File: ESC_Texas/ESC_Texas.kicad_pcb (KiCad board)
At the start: 4 copper layers, 118 x 73.2 mm, 165 parts, among them IC1 nRF52840-QFAA-F-R7, IC10 UCC21331CQDRQ1, IC11 LM3480IM3-3.3_NOPB, IC2 UCC21331CQDRQ1, IC3 AD8411AWBRZ, IC4 MC78L05ACHT1G, IC5 AD8411AWBRZ, IC6 MC78L05ACHT1G, IC7 UCC21331CQDRQ1, IC8 AD8411AWBRZ, IC9 MC78L05ACHT1G, J1 Battery-, J10 Conn_01x03_Pin, J11 Conn_01x02_Pin, J12 Conn_01x02, J13 Conn_01x06_Pin, J14 Conn_01x04_Pin, J15 Conn_01x04_Pin, J16 Conn_01x07_Pin, J2 Conn_01x08_Pin, J3 Motor, J4 Battery+, J5 Conn_01x03_Pin, J6 Conn_01x03_Pin, J7 Conn_01x03_Pin, J8 Conn_01x03_Pin, J9 Conn_01x03_Pin, Q1 IPD100N06S4, Q2 IPD100N06S4, Q3 IPD100N06S4, Q4 IPD100N06S4, Q5 IPD100N06S4, Q6 IPD100N06S4, U1 MCP2515-xSO, U2 TJA1051T, X1 C115962, Y1 CM7V-T1A-32.768kHz, Y2 32MHz

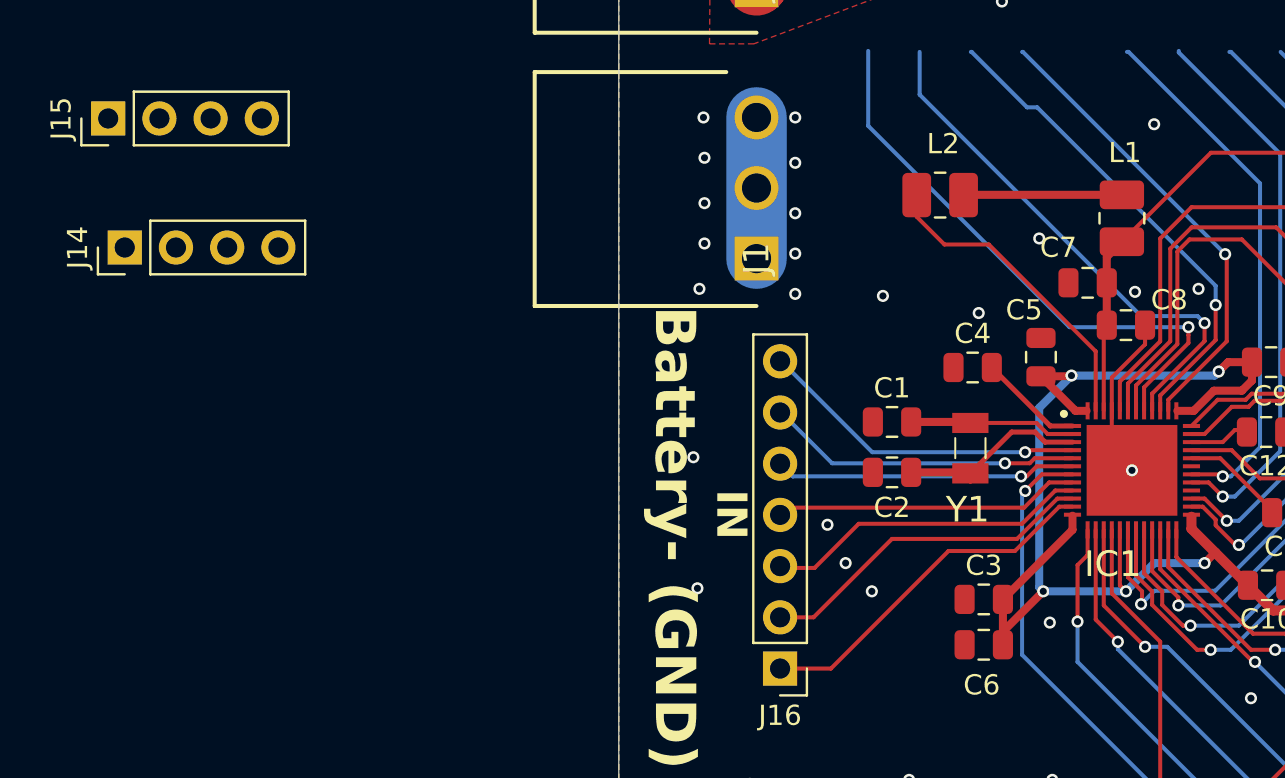
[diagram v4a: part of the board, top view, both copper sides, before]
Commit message: Testpoints instead of hearders
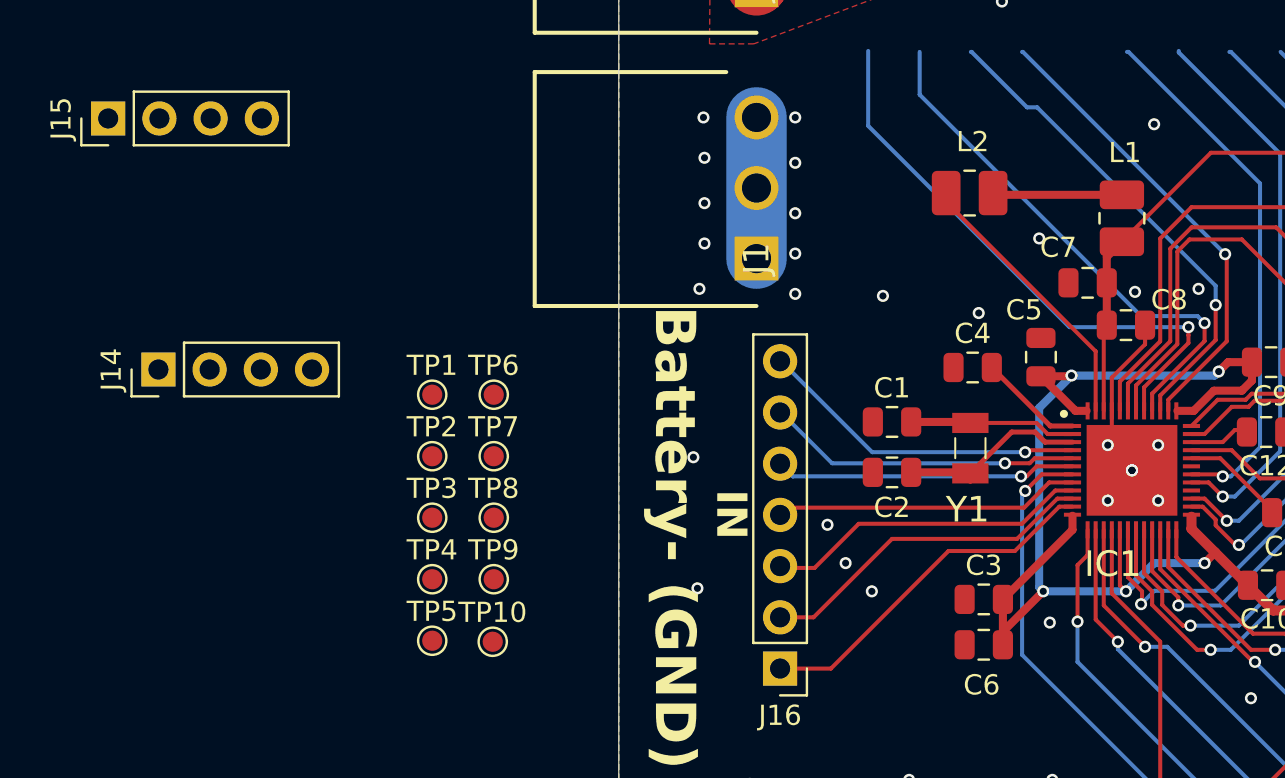
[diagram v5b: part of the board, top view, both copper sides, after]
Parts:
- added TP1: TestPoint, TestPoint:TestPoint_Pad_D1.0mm, F.Cu at (82.8, 111.5)
- added TP10: TestPoint, TestPoint:TestPoint_Pad_D1.0mm, F.Cu at (85.8, 123.8)
- added TP2: TestPoint, TestPoint:TestPoint_Pad_D1.0mm, F.Cu at (82.8, 114.5)
- added TP3: TestPoint, TestPoint:TestPoint_Pad_D1.0mm, F.Cu at (82.8, 117.6)
- added TP4: TestPoint, TestPoint:TestPoint_Pad_D1.0mm, F.Cu at (82.8, 120.7)
- added TP5: TestPoint, TestPoint:TestPoint_Pad_D1.0mm, F.Cu at (82.8, 123.7)
- added TP6: TestPoint, TestPoint:TestPoint_Pad_D1.0mm, F.Cu at (85.8, 111.5)
- added TP7: TestPoint, TestPoint:TestPoint_Pad_D1.0mm, F.Cu at (85.8, 114.5)
- added TP8: TestPoint, TestPoint:TestPoint_Pad_D1.0mm, F.Cu at (85.8, 117.6)
- added TP9: TestPoint, TestPoint:TestPoint_Pad_D1.0mm, F.Cu at (85.8, 120.7)
- moved J14 6.28 mm to (69.2, 110.2)
- moved L2 1.47 mm to (109.4, 101.5)
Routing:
- net Net-(IC1-DCC): track 15.7 -> 13.9 mm
- net Net-(L1-Pad2): track 7.86 -> 6.42 mm
- net GND: vias 202 -> 207

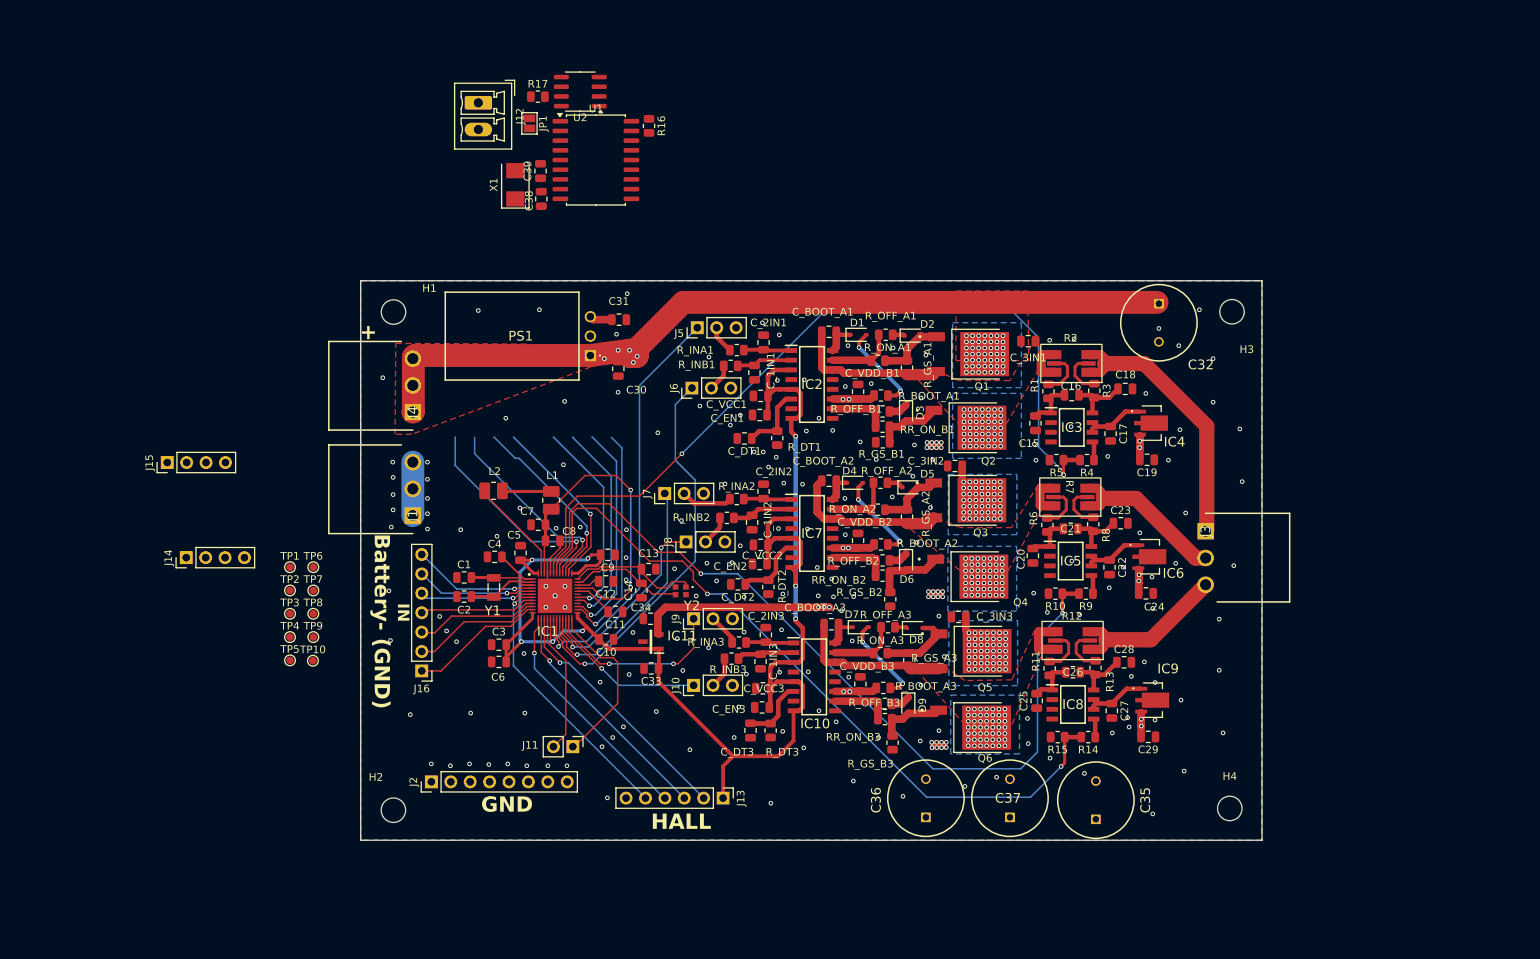
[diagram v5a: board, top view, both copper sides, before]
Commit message: test points and CAN
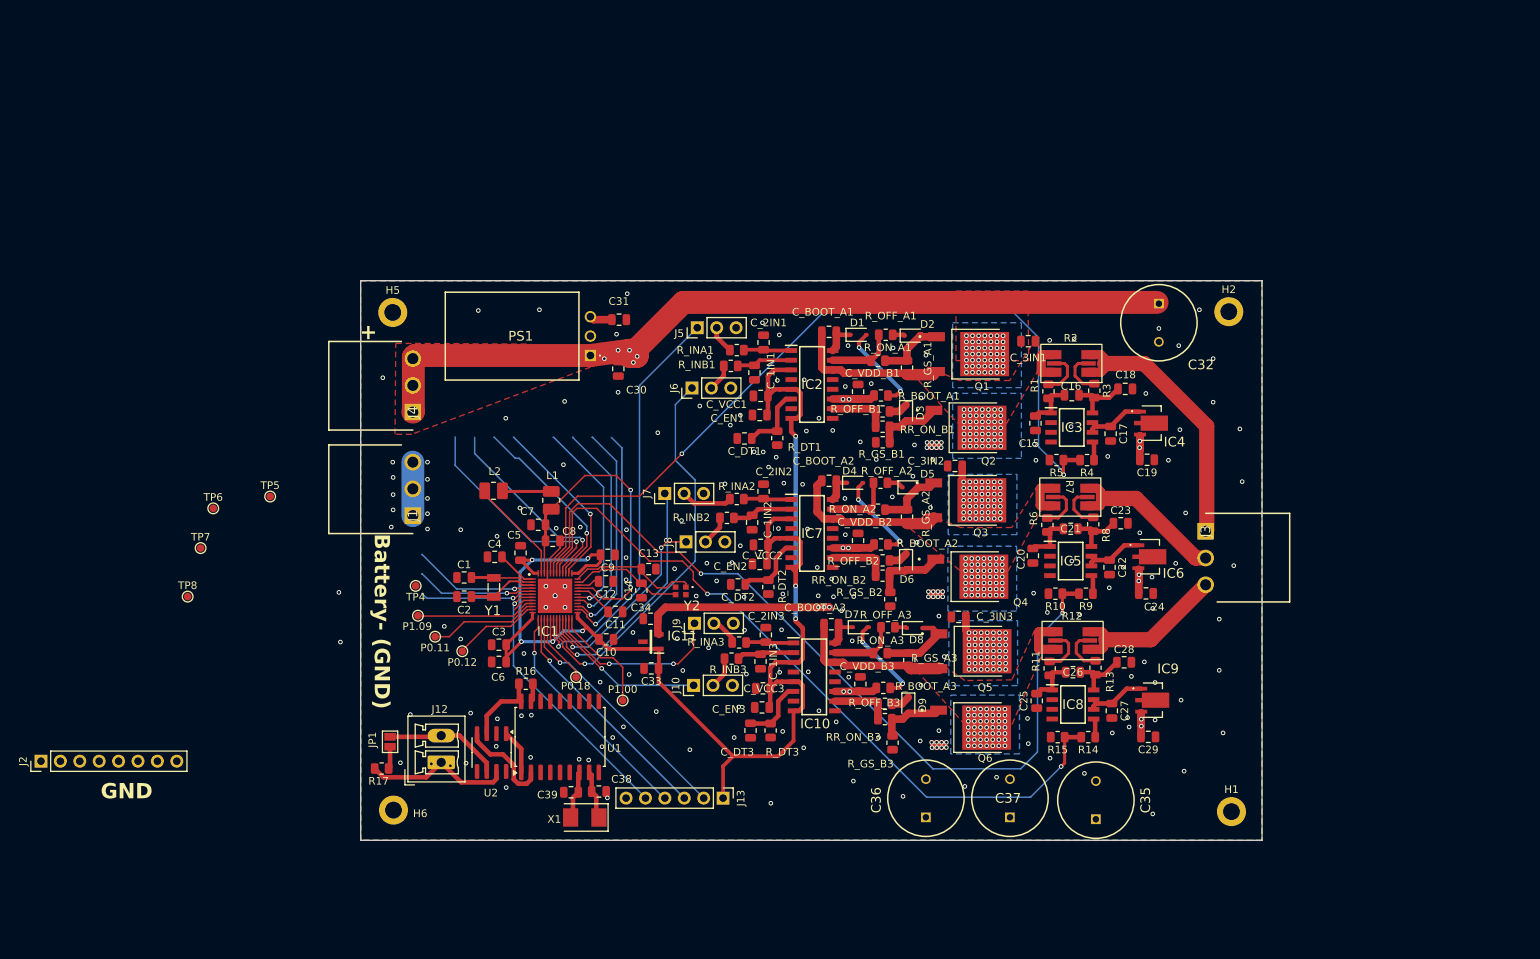
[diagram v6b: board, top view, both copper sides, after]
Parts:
- removed H3, H4: MountingHole, MountingHole:MountingHole_3.2mm_M3
- removed J11: Conn_01x02_Pin, Connector_PinHeader_2.54mm:PinHeader_1x02_P2.54mm_Vertical
- removed J14, J15: Conn_01x04_Pin, Connector_PinHeader_2.54mm:PinHeader_1x04_P2.54mm_Vertical
- removed J16: Conn_01x07_Pin, Connector_PinHeader_2.54mm:PinHeader_1x07_P2.54mm_Vertical
- added H5: MountingHole_Pad, MountingHole:MountingHole_2.2mm_M2_DIN965_Pad, F.Cu at (96.2, 78.2)
- added H6: MountingHole_Pad, MountingHole:MountingHole_2.2mm_M2_DIN965_Pad, F.Cu at (96.3, 143.3)
- H1, H2: value MountingHole -> MountingHole_Pad; footprint MountingHole:MountingHole_3.2mm_M3 -> MountingHole:MountingHole_2.2mm_M2_DIN965_Pad
- moved H1 127.7 mm to (206.0, 143.5)
- moved H2 127.4 mm to (205.7, 78.0)
- moved R17 90.3 mm to (94.8, 137.9), turned to 180 degrees
- moved U2 87.3 mm to (109.1, 135.8), turned to -90 degrees
- moved J12 86.5 mm to (102.5, 137.1), turned to 90 degrees
- moved X1 83.3 mm to (121.3, 144.3), turned to 180 degrees
- moved JP1 83.0 mm to (95.9, 134.4), turned to 90 degrees
- moved C39 81.4 mm to (119.5, 141.0), turned to 180 degrees
- moved C38 77.9 mm to (123.2, 140.9), turned to 0 degrees
- moved U1 75.7 mm to (118.1, 133.7), turned to 90 degrees
- moved R16 74.8 mm to (113.6, 126.8), turned to 0 degrees
- moved J2 51.2 mm to (50.1, 136.9)
- moved P1.00 41.3 mm to (126.3, 128.9)
- moved P0.18 34.5 mm to (120.2, 125.9)
- moved P0.12 25.1 mm to (105.3, 122.5), turned to 180 degrees
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- renumbered TP2 to P0.11, TP1 to P0.12, TP10 to P0.18, TP9 to P1.00, TP3 to P1.09
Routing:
- net Net-(J12-Pin_1): track 0.00 -> 19.5 mm
- net Net-(J12-Pin_2): track 0.00 -> 15.3 mm
- net Net-(U1-RXCAN): track 0.00 -> 12.6 mm
- net P1.08: track 15.4 -> 2.92 mm
- net VDD: track 193.0 -> 203.0 mm
- net P0.18: track 18.5 -> 9.25 mm
- net P1.00: track 22.8 -> 14.4 mm
- net Net-(U1-OSC1): track 0.00 -> 6.43 mm
- net Net-(U1-OSC2): track 0.00 -> 6.38 mm
- net P0.12: track 17.8 -> 11.5 mm
- net Net-(U1-TXCAN): track 0.00 -> 5.89 mm
- net Net-(JP1-A): track 0.00 -> 2.93 mm
- net P0.11: track 16.9 -> 14.4 mm
- net Net-(U1-~{RESET}): track 0.00 -> 2.40 mm
- net P0.24: track 24.6 -> 24.0 mm
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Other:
- board text removed: "HALL"
- board text removed: "IN"
